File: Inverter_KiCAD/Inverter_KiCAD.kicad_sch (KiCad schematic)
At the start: 0 parts

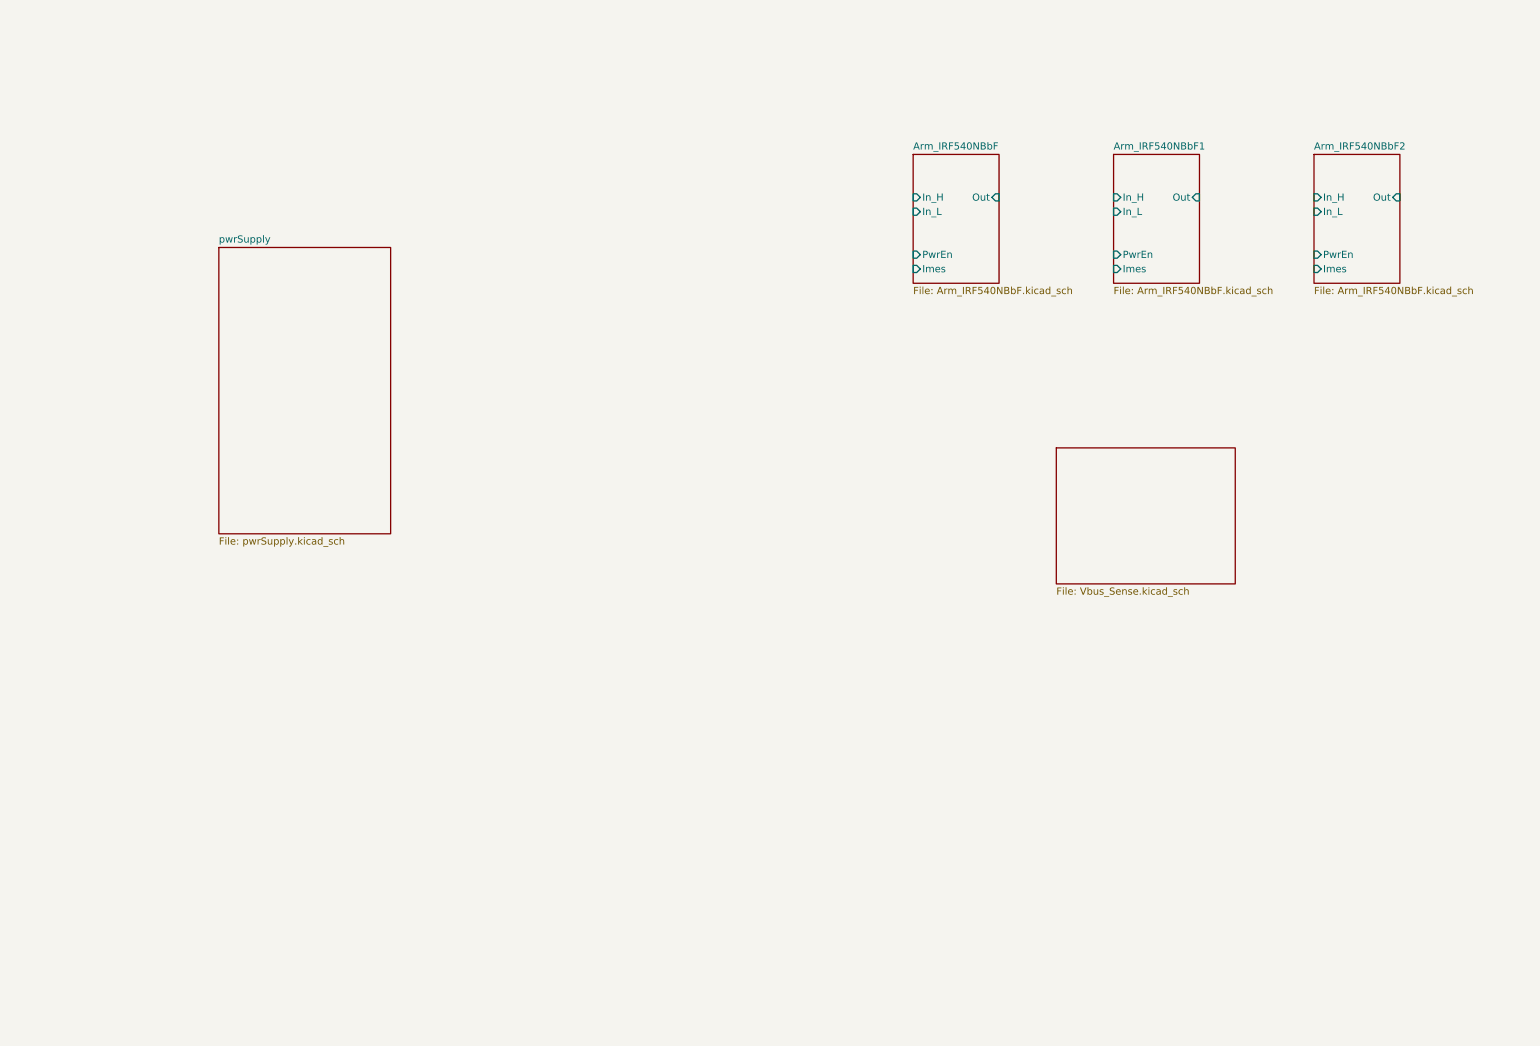
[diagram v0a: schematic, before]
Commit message: update schematic
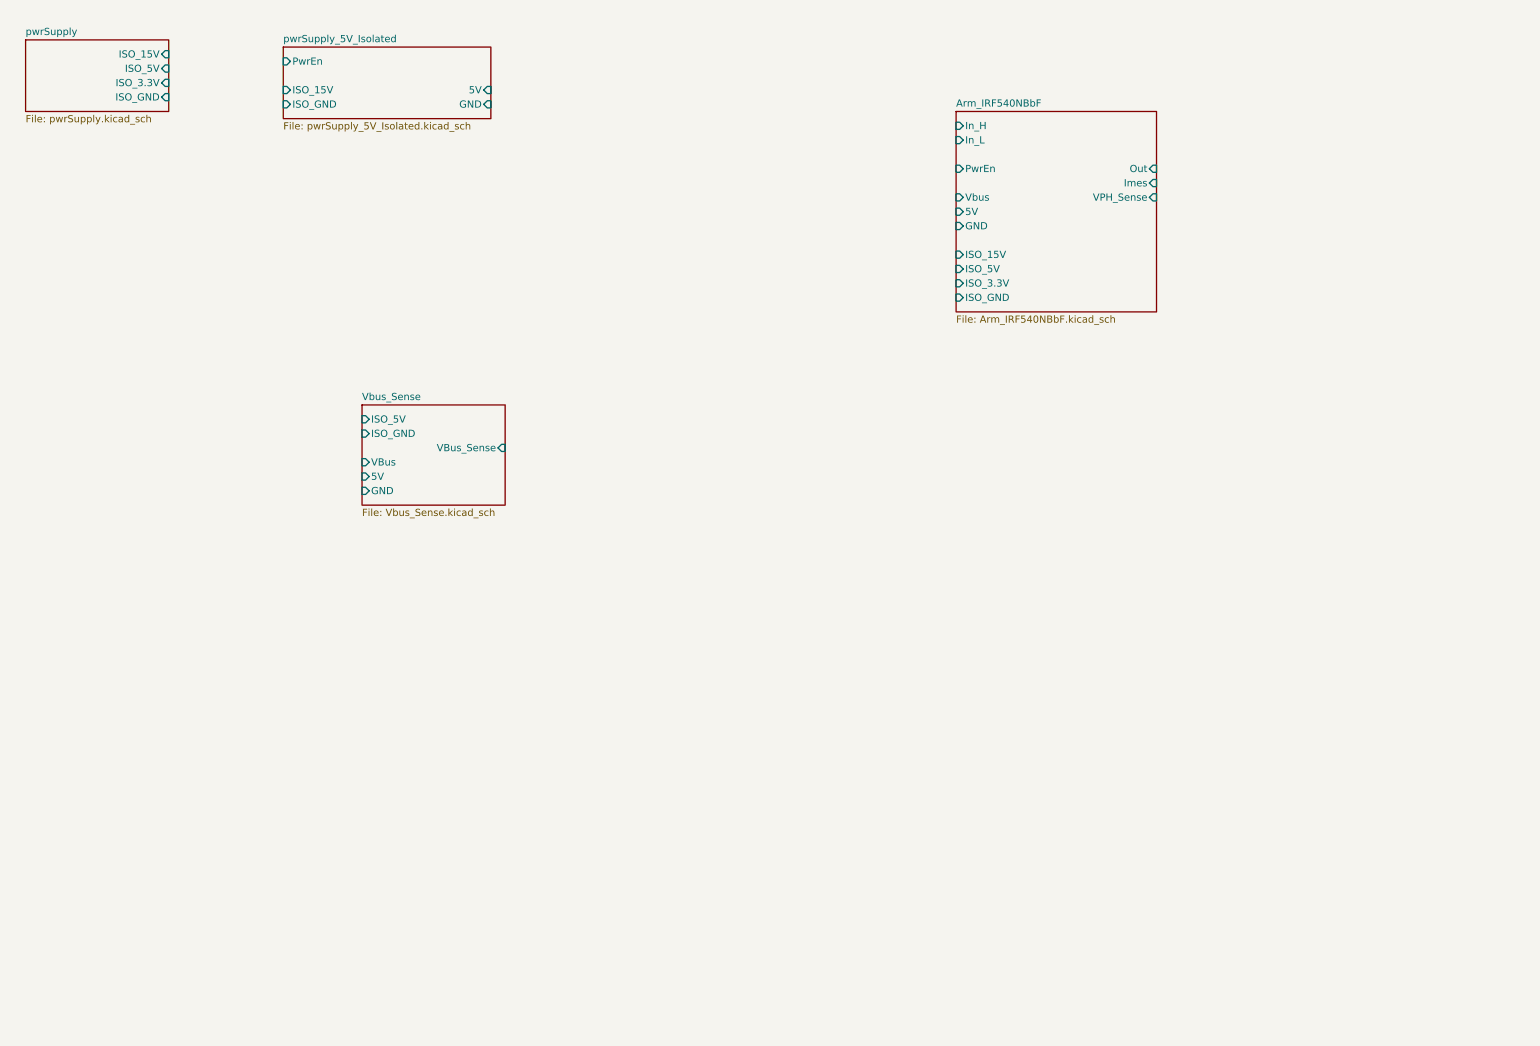
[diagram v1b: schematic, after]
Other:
- removed sheet Arm_IRF540NBbF1
- removed sheet Arm_IRF540NBbF2
- added sheet pwrSupply_5V_Isolated (pwrSupply_5V_Isolated.kicad_sch)
- sheet Arm_IRF540NBbF ports: added 5V, GND, ISO_15V, ISO_3.3V, ISO_5V, ISO_GND, VPH_Sense, Vbus; removed none
- sheet Vbus_Sense ports: added 5V, GND, ISO_5V, ISO_GND, VBus, VBus_Sense; removed none
- sheet pwrSupply ports: added ISO_15V, ISO_3.3V, ISO_5V, ISO_GND; removed none
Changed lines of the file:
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@@
 (kicad_sch (version 20230121) (generator eeschema)
   (paper "A4")
-  (sheet (at 50.8 55.88) (size 30.48 50.8) (fields_autoplaced)
+  (sheet (at 16.51 19.05) (size 25.4 12.7) (fields_autoplaced)
     (stroke (width 0.1524) (type solid))
     (fill (color 0 0 0 0.0000))
-    (property "Sheetname" "pwrSupply" (at 50.8 55.1684 0)
+    (property "Sheetname" "pwrSupply" (at 16.51 18.3384 0)
       (effects (font (size 1.27 1.27)) (justify left bottom))
     )
-    (property "Sheetfile" "pwrSupply.kicad_sch" (at 50.8 107.2646 0)
+    (property "Sheetfile" "pwrSupply.kicad_sch" (at 16.51 32.3346 0)
       (effects (font (size 1.27 1.27)) (justify left top))
     )
-    (property "Field2" "" (at 50.8 55.88 0)
+    (property "Field2" "" (at 16.51 19.05 0)
       (effects (font (size 1.27 1.27)) hide)
+    )
+    (pin "ISO_5V" input (at 41.91 24.13 0)
+      (effects (font (size 1.27 1.27)) (justify right))
+    )
+    (pin "ISO_3.3V" input (at 41.91 26.67 0)
+      (effects (font (size 1.27 1.27)) (justify right))
+    )
+    (pin "ISO_GND" input (at 41.91 29.21 0)
+      (effects (font (size 1.27 1.27)) (justify right))
+    )
+    (pin "ISO_15V" input (at 41.91 21.59 0)
+      (effects (font (size 1.27 1.27)) (justify right))
     )
     (instances
@@
     )
   )
-  (sheet (at 245.11 39.37) (size 15.24 22.86) (fields_autoplaced)
+  (sheet (at 62.23 20.32) (size 36.83 12.7) (fields_autoplaced)
     (stroke (width 0.1524) (type solid))
     (fill (color 0 0 0 0.0000))
-    (property "Sheetname" "Arm_IRF540NBbF2" (at 245.11 38.6584 0)
+    (property "Sheetname" "pwrSupply_5V_Isolated" (at 62.23 19.6084 0)
       (effects (font (size 1.27 1.27)) (justify left bottom))
     )
-    (property "Sheetfile" "Arm_IRF540NBbF.kicad_sch" (at 245.11 62.8146 0)
+    (property "Sheetfile" "pwrSupply_5V_Isolated.kicad_sch" (at 62.23 33.6046 0)
       (effects (font (size 1.27 1.27)) (justify left top))
     )
-    (pin "Out" input (at 260.35 46.99 0)
+    (property "Field2" "" (at 62.23 20.32 0)
+      (effects (font (size 1.27 1.27)) hide)
+    )
+    (pin "ISO_15V" input (at 62.23 27.94 180)
+      (effects (font (size 1.27 1.27)) (justify left))
+    )
+    (pin "PwrEn" input (at 62.23 22.86 180)
+      (effects (font (size 1.27 1.27)) (justify left))
+    )
+    (pin "ISO_GND" input (at 62.23 30.48 180)
+      (effects (font (size 1.27 1.27)) (justify left))
+    )
+    (pin "5V" input (at 99.06 27.94 0)
       (effects (font (size 1.27 1.27)) (justify right))
     )
-    (pin "Imes" input (at 245.11 59.69 180)
-      (effects (font (size 1.27 1.27)) (justify left))
-    )
-    (pin "In_L" input (at 245.11 49.53 180)
-      (effects (font (size 1.27 1.27)) (justify left))
-    )
-    (pin "In_H" input (at 245.11 46.99 180)
-      (effects (font (size 1.27 1.27)) (justify left))
-    )
-    (pin "PwrEn" input (at 245.11 57.15 180)
-      (effects (font (size 1.27 1.27)) (justify left))
+    (pin "GND" input (at 99.06 30.48 0)
+      (effects (font (size 1.27 1.27)) (justify right))
     )
     (instances
       (project "Inverter_KiCAD"
-        (path "/5e6c1e3f-0815-454a-8acb-8e3e2d064875" (page "4"))
+        (path "/5e6c1e3f-0815-454a-8acb-8e3e2d064875" (page "7"))
       )
     )
   )
-  (sheet (at 199.39 91.44) (size 31.75 24.13) (fields_autoplaced)
+  (sheet (at 76.2 83.82) (size 25.4 17.78) (fields_autoplaced)
     (stroke (width 0.1524) (type solid))
     (fill (color 0 0 0 0.0000))
-    (property "Sheetname" "Vbus_Sense" (at 199.39 90.7284 0)
-      (effects (font (size 1.27 1.27)) (justify left bottom) hide)
+    (property "Sheetname" "Vbus_Sense" (at 76.2 83.1084 0)
+      (effects (font (size 1.27 1.27)) (justify left bottom))
     )
-    (property "Sheetfile" "Vbus_Sense.kicad_sch" (at 199.39 116.1546 0)
+    (property "Sheetfile" "Vbus_Sense.kicad_sch" (at 76.2 102.1846 0)
       (effects (font (size 1.27 1.27)) (justify left top))
+    )
+    (pin "VBus_Sense" input (at 101.6 91.44 0)
+      (effects (font (size 1.27 1.27)) (justify right))
+    )
+    (pin "GND" input (at 76.2 99.06 180)
+      (effects (font (size 1.27 1.27)) (justify left))
+    )
+    (pin "VBus" input (at 76.2 93.98 180)
+      (effects (font (size 1.27 1.27)) (justify left))
+    )
+    (pin "5V" input (at 76.2 96.52 180)
+      (effects (font (size 1.27 1.27)) (justify left))
+    )
+    (pin "ISO_5V" input (at 76.2 86.36 180)
+      (effects (font (size 1.27 1.27)) (justify left))
+    )
+    (pin "ISO_GND" input (at 76.2 88.9 180)
+      (effects (font (size 1.27 1.27)) (justify left))
     )
     (instances
@@
     )
   )
-  (sheet (at 173.99 39.37) (size 15.24 22.86) (fields_autoplaced)
+  (sheet (at 181.61 31.75) (size 35.56 35.56) (fields_autoplaced)
     (stroke (width 0.1524) (type solid))
     (fill (color 0 0 0 0.0000))
-    (property "Sheetname" "Arm_IRF540NBbF" (at 173.99 38.6584 0)
+    (property "Sheetname" "Arm_IRF540NBbF" (at 181.61 31.0384 0)
       (effects (font (size 1.27 1.27)) (justify left bottom))
     )
-    (property "Sheetfile" "Arm_IRF540NBbF.kicad_sch" (at 173.99 62.8146 0)
+    (property "Sheetfile" "Arm_IRF540NBbF.kicad_sch" (at 181.61 67.8946 0)
       (effects (font (size 1.27 1.27)) (justify left top))
     )
-    (pin "Out" input (at 189.23 46.99 0)
+    (pin "Out" input (at 217.17 41.91 0)
       (effects (font (size 1.27 1.27)) (justify right))
     )
-    (pin "Imes" input (at 173.99 59.69 180)
+    (pin "Imes" input (at 217.17 44.45 0)
+      (effects (font (size 1.27 1.27)) (justify right))
+    )
+    (pin "ISO_GND" input (at 181.61 64.77 180)
       (effects (font (size 1.27 1.27)) (justify left))
     )
-    (pin "In_L" input (at 173.99 49.53 180)
+    (pin "ISO_3.3V" input (at 181.61 62.23 180)
       (effects (font (size 1.27 1.27)) (justify left))
     )
-    (pin "In_H" input (at 173.99 46.99 180)
+    (pin "GND" input (at 181.61 52.07 180)
       (effects (font (size 1.27 1.27)) (justify left))
     )
-    (pin "PwrEn" input (at 173.99 57.15 180)
+    (pin "PwrEn" input (at 181.61 41.91 180)
+      (effects (font (size 1.27 1.27)) (justify left))
+    )
+    (pin "ISO_15V" input (at 181.61 57.15 180)
+      (effects (font (size 1.27 1.27)) (justify left))
+    )
+    (pin "In_L" input (at 181.61 36.83 180)
+      (effects (font (size 1.27 1.27)) (justify left))
+    )
+    (pin "In_H" input (at 181.61 34.29 180)
+      (effects (font (size 1.27 1.27)) (justify left))
+    )
+    (pin "5V" input (at 181.61 49.53 180)
+      (effects (font (size 1.27 1.27)) (justify left))
+    )
+    (pin "ISO_5V" input (at 181.61 59.69 180)
+      (effects (font (size 1.27 1.27)) (justify left))
+    )
+    (pin "VPH_Sense" input (at 217.17 46.99 0)
+      (effects (font (size 1.27 1.27)) (justify right))
+    )
+    (pin "Vbus" input (at 181.61 46.99 180)
       (effects (font (size 1.27 1.27)) (justify left))
     )
@@
       )
     )
-  )
-  (sheet (at 209.55 39.37) (size 15.24 22.86) (fields_autoplaced)
-    (stroke (width 0.1524) (type solid))
-    (fill (color 0 0 0 0.0000))
-    (property "Sheetname" "Arm_IRF540NBbF1" (at 209.55 38.6584 0)
-      (effects (font (size 1.27 1.27)) (justify left bottom))
-    )
-    (property "Sheetfile" "Arm_IRF540NBbF.kicad_sch" (at 209.55 62.8146 0)
-      (effects (font (size 1.27 1.27)) (justify left top))
-    )
-    (pin "Out" input (at 224.79 46.99 0)
-      (effects (font (size 1.27 1.27)) (justify right))
-    )
-    (pin "Imes" input (at 209.55 59.69 180)
-      (effects (font (size 1.27 1.27)) (justify left))
-    )
-    (pin "In_L" input (at 209.55 49.53 180)
-      (effects (font (size 1.27 1.27)) (justify left))
-    )
-    (pin "In_H" input (at 209.55 46.99 180)
-      (effects (font (size 1.27 1.27)) (justify left))
-    )
-    (pin "PwrEn" input (at 209.55 57.15 180)
-      (effects (font (size 1.27 1.27)) (justify left))
-    )
-    (instances
-      (project "Inverter_KiCAD"
-        (path "/5e6c1e3f-0815-454a-8acb-8e3e2d064875" (page "3"))
-      )
-    )

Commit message: update schematic
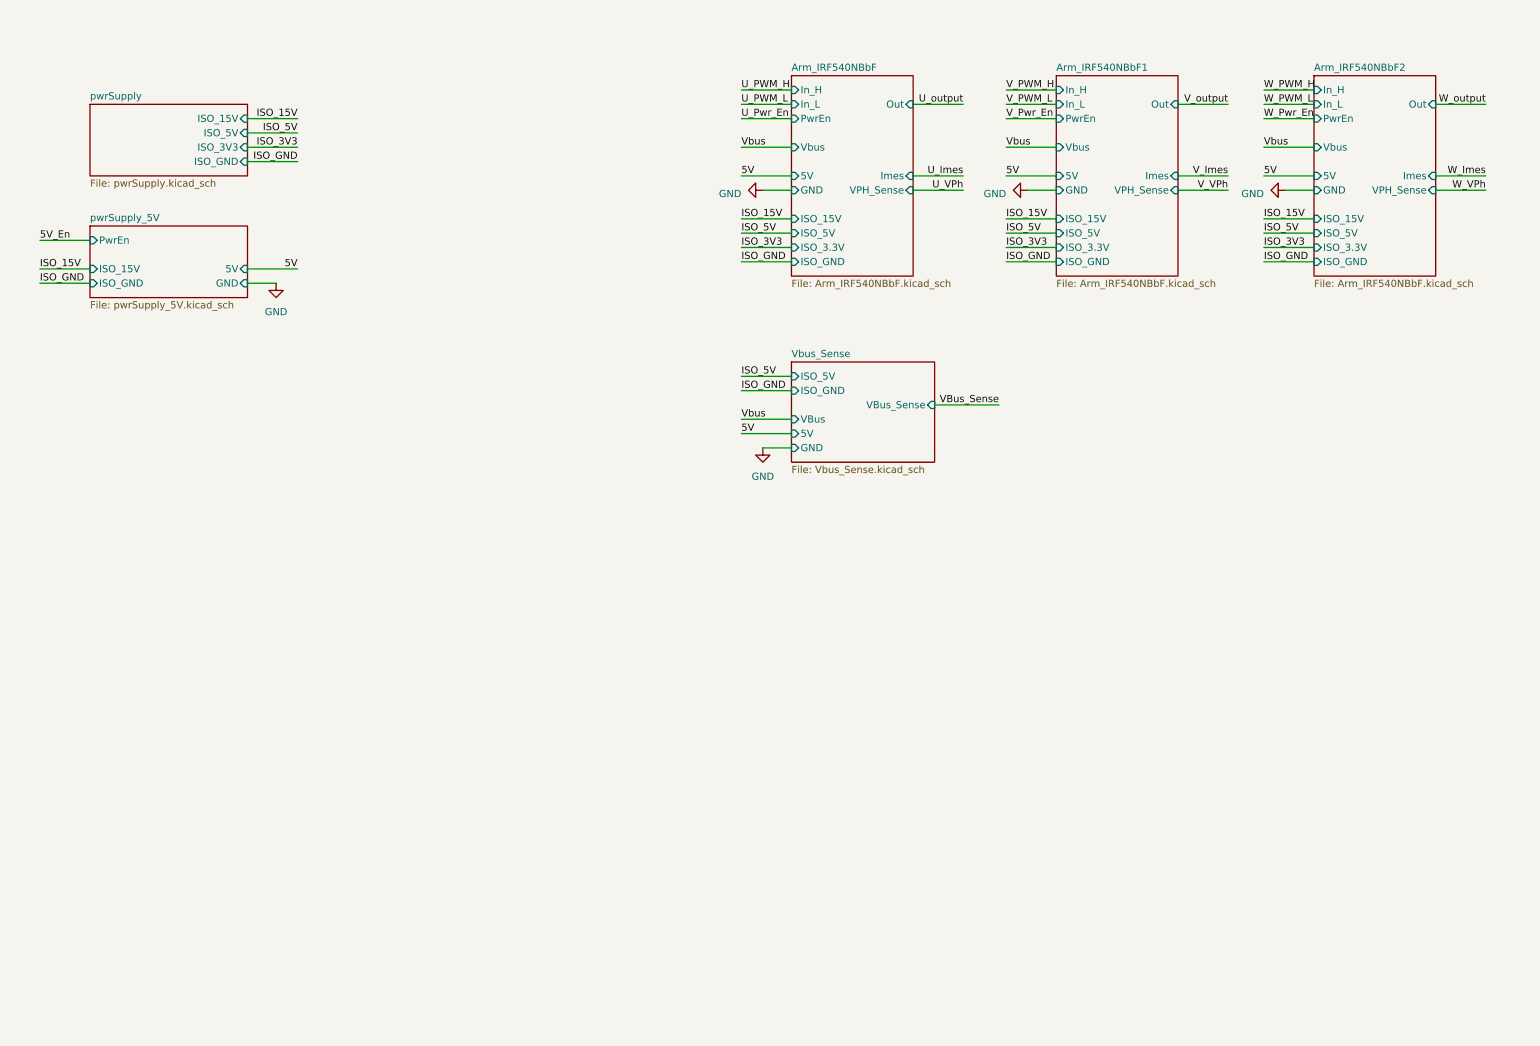
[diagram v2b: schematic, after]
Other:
- sheet pwrSupply_5V_Isolated renamed pwrSupply_5V
- added sheet Arm_IRF540NBbF1 (Arm_IRF540NBbF.kicad_sch)
- added sheet Arm_IRF540NBbF2 (Arm_IRF540NBbF.kicad_sch)
- sheet pwrSupply ports: added ISO_3V3; removed ISO_3.3V
- sheet pwrSupply_5V: file pwrSupply_5V_Isolated.kicad_sch -> pwrSupply_5V.kicad_sch

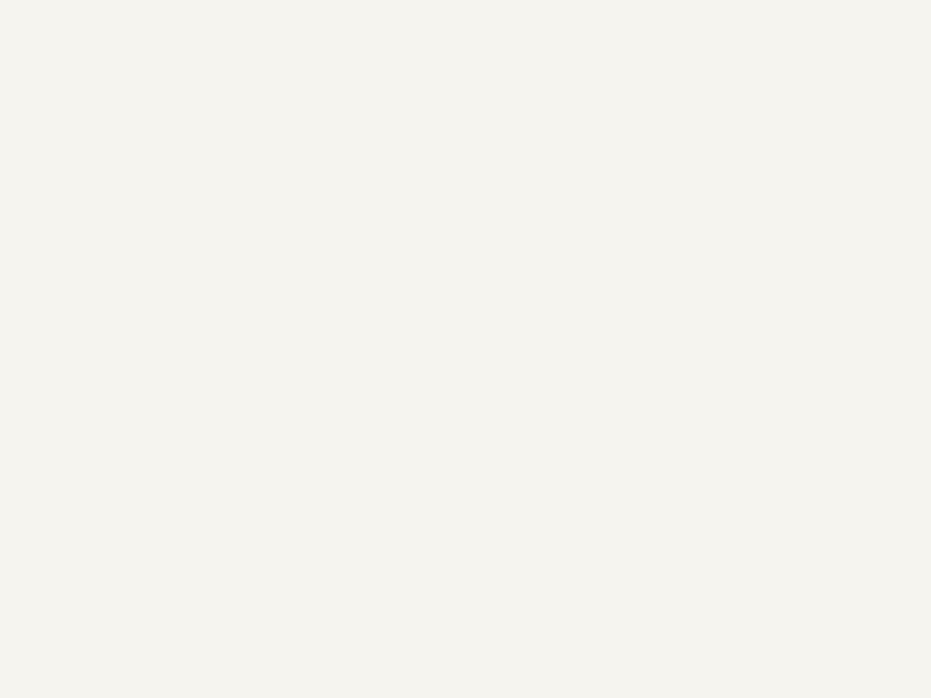
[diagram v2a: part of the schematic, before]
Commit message: update schematic
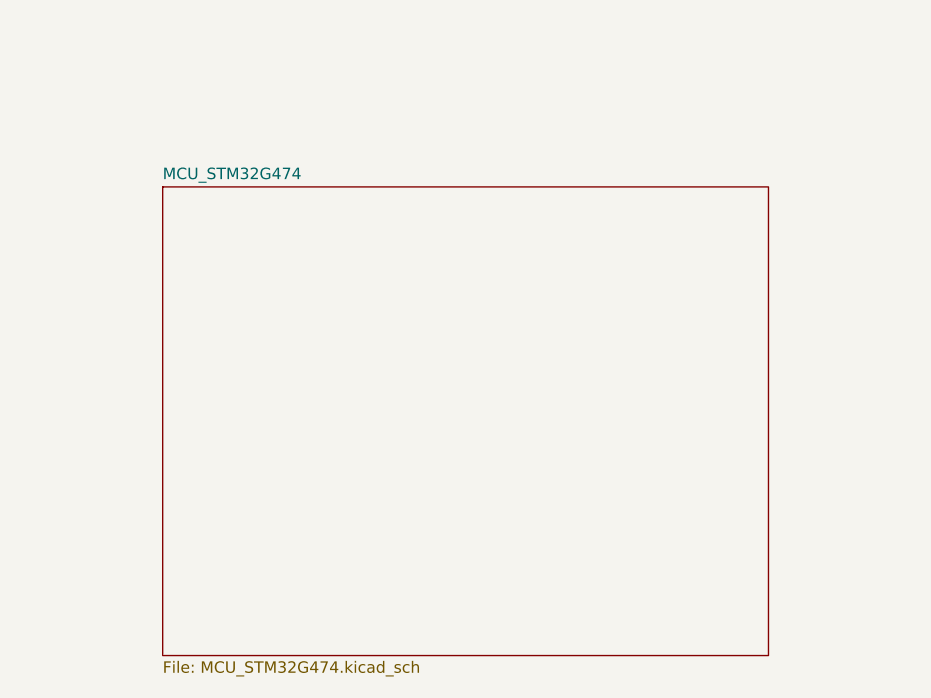
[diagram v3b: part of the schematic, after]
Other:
- added sheet MCU_STM32G474 (MCU_STM32G474.kicad_sch)
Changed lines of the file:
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@@
+    )
+  )
+  (sheet (at 46.99 91.44) (size 67.31 52.07) (fields_autoplaced)
+    (stroke (width 0.1524) (type solid))
+    (fill (color 0 0 0 0.0000))
+    (property "Sheetname" "MCU_STM32G474" (at 46.99 90.7284 0)
+      (effects (font (size 1.27 1.27)) (justify left bottom))
+    )
+    (property "Sheetfile" "MCU_STM32G474.kicad_sch" (at 46.99 144.0946 0)
+      (effects (font (size 1.27 1.27)) (justify left top))
+    )
+    (instances
+      (project "Inverter_KiCAD"
+        (path "/5e6c1e3f-0815-454a-8acb-8e3e2d064875" (page "8"))
+      )
     )
   )
